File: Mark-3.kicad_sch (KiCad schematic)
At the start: 11 parts

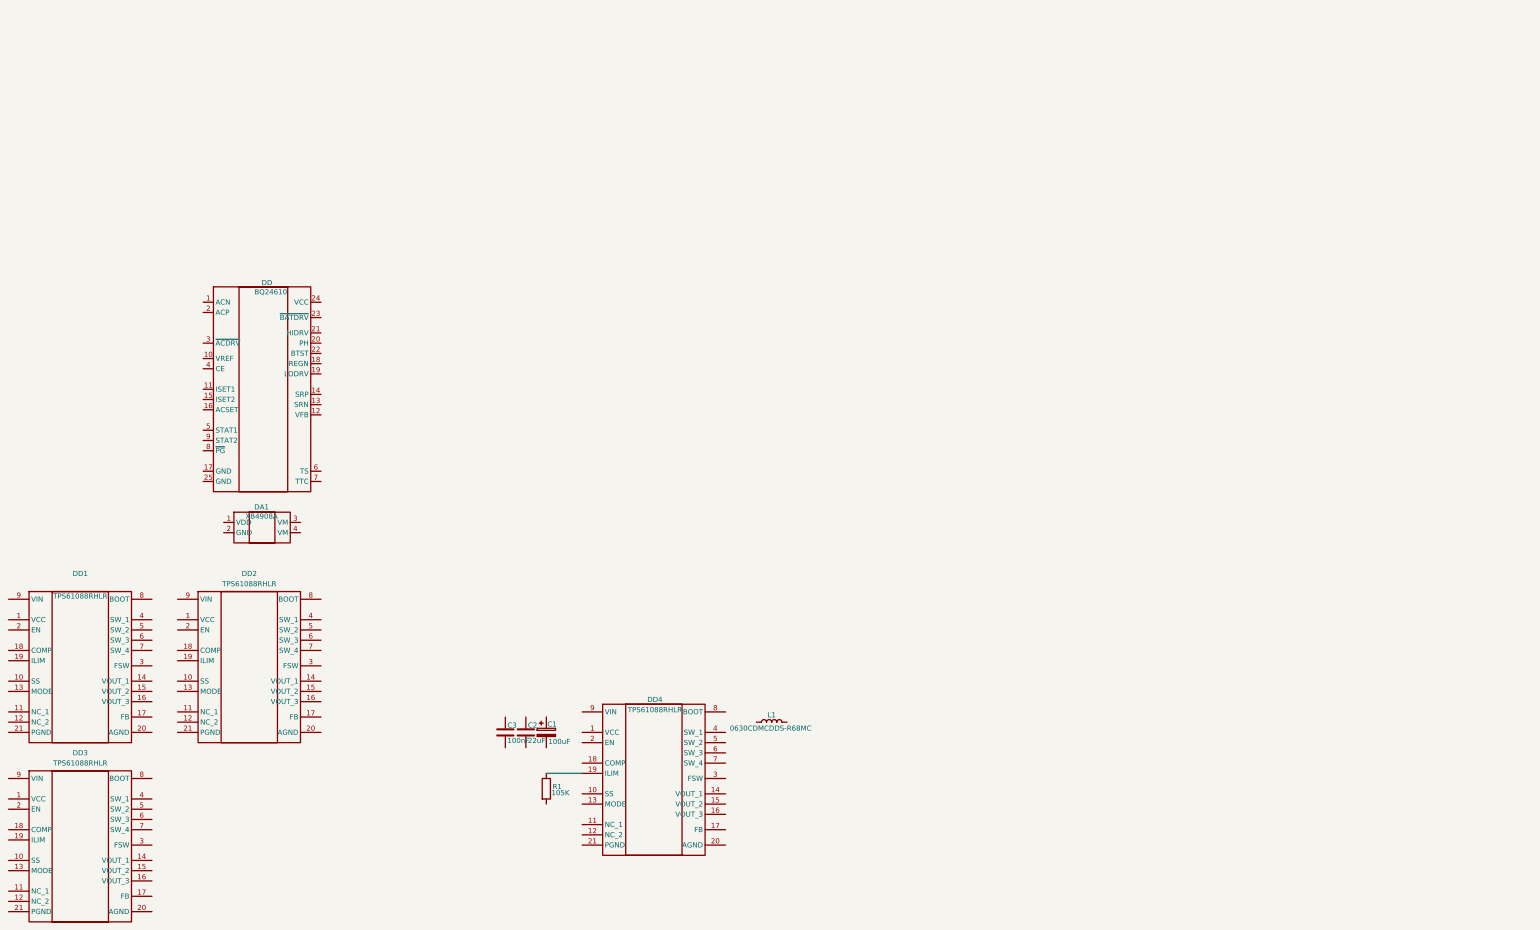
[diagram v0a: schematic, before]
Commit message: DC-DC and battery protection circuit done, partly done charger module
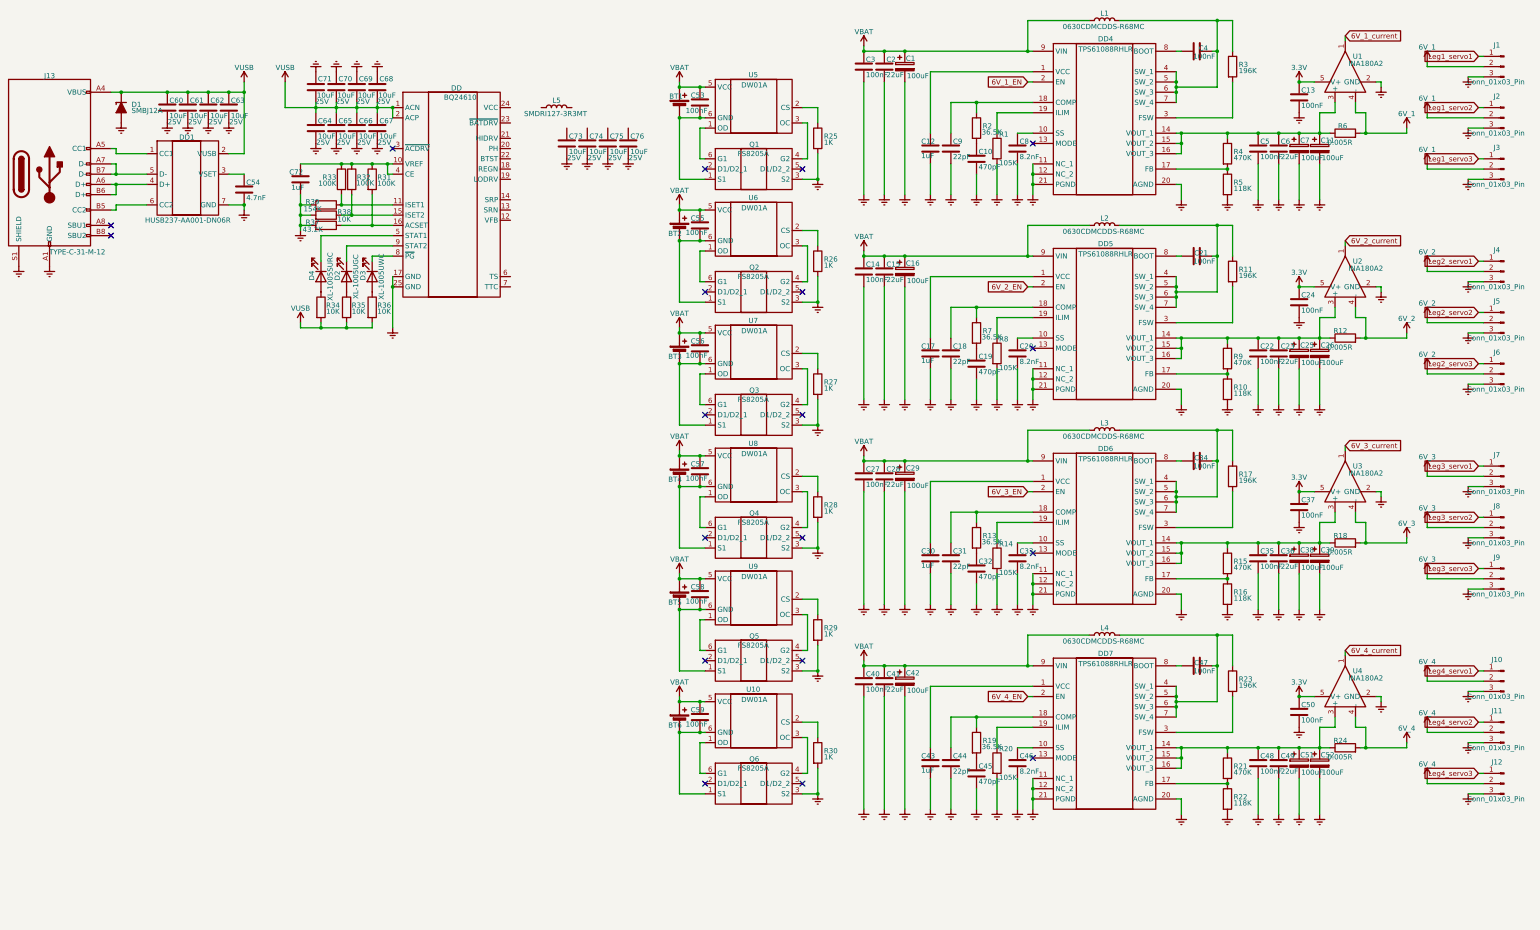
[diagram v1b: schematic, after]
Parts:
- removed DA1: XB4908A, XB4908A:XB4908A, symbol XB4908A:XB4908A
- removed DD1, DD2, DD3: TPS61088RHLR, TPS61088RHLR:TPS61088RHLR, symbol TPS61088RHLR:TPS61088RHLR
- added BT1, BT2, BT3, BT4, BT5, BT6: Battery_Cell, Battery:BatteryHolder_Keystone_1042_1x18650, symbol Device:Battery_Cell
- added C10, C19, C32, C45: 470pF, Capacitor_SMD:C_0402_1005Metric, symbol Device:C
- added C11, C16, C25, C26, C29, C38, C39, C42, C51, C52, C7: 100uF, Capacitor_Tantalum_SMD:CP_EIA-3528-21_Kemet-B, symbol Device:C_Polarized
- added C12, C17, C30, C43, C72: 1uF, Capacitor_SMD:C_0402_1005Metric, symbol Device:C
- added C13, C14, C21, C22, C24, C27, C34, C35, C37, C4, C40, C47, C48, C5, C50, C53, C55, C56, C57, C58, C59: 100nF, Capacitor_SMD:C_0402_1005Metric, symbol Device:C
- added C15, C23, C28, C36, C41, C49, C6: 22uF, Capacitor_SMD:C_0805_2012Metric, symbol Device:C
- added C18, C31, C44, C9: 22pF, Capacitor_SMD:C_0402_1005Metric, symbol Device:C
- added C20, C33, C46, C8: 8.2nF, Capacitor_SMD:C_0402_1005Metric, symbol Device:C
- added C54: 4.7nF, Capacitor_SMD:C_0402_1005Metric, symbol Device:C
- added C60, C61, C62, C63, C64, C65, C66, C67, C68, C69, C70, C71, C73, C74, C75, C76: 10uF, Capacitor_SMD:C_0805_2012Metric, symbol Device:C
- added D1: SMBJ12A, PCM_Diode_SMD_AKL:D_SMB, symbol PCM_Diode_TVS_AKL:SMBJ12A
- added D2: XL-1005UGC, LED_SMD:LED_0402_1005Metric, symbol Device:LED
- added D3: XL-1005UWC, LED_SMD:LED_0402_1005Metric, symbol Device:LED
- added D4: XL-1005SURC, LED_SMD:LED_0402_1005Metric, symbol Device:LED
- added DD1: HUSB237-AA001-DN06R, HUSB237-AA001-DN06R:HUSB237-AA001-DN06R, symbol HUSB237-AA001-DN06R:HUSB237-AA001-DN06R
- added DD5, DD6, DD7: TPS61088RHLR, TPS61088RHLR:TPS61088RHLR, symbol TPS61088RHLR:TPS61088RHLR
- added J1, J10, J11, J12, J2, J3, J4, J5, J6, J7, J8, J9: Conn_01x03_Pin, Connector_PinHeader_2.54mm:PinHeader_1x03_P2.54mm_Vertical, symbol Connector:Conn_01x03_Pin
- added J13: TYPE-C-31-M-12, Connector_USB:USB_C_Receptacle_G-Switch_GT-USB-7010ASV, symbol Connector:USB_C_Receptacle_USB2.0_16P
- added L2, L3, L4: 0630CDMCDDS-R68MC, Inductor_SMD:L_Sunlord_MWSA0603S, symbol Device:L
- added L5: SMDRI127-3R3MT, Inductor_SMD:L_SXN_SMDRI127, symbol Device:L
- added Q1, Q2, Q3, Q4, Q5, Q6: FS8205A, FS8205A:FS8205A, symbol FS8205A:FS8205A
- added R10, R16, R22, R5: 118K, PCM_Resistor_SMD_AKL:R_0402_1005Metric, symbol Device:R
- added R11, R17, R23, R3: 196K, PCM_Resistor_SMD_AKL:R_0402_1005Metric, symbol Device:R
- added R12, R18, R24, R6: 0.005R, PCM_Resistor_SMD_AKL:R_1206_3216Metric, symbol Device:R
- added R13, R19, R2, R7: 36.5K, PCM_Resistor_SMD_AKL:R_0402_1005Metric, symbol Device:R
- added R14, R20, R8: 105K, PCM_Resistor_SMD_AKL:R_0402_1005Metric, symbol Device:R
- added R15, R21, R4, R9: 470K, PCM_Resistor_SMD_AKL:R_0402_1005Metric, symbol Device:R
- added R25, R26, R27, R28, R29, R30: 1K, PCM_Resistor_SMD_AKL:R_0402_1005Metric, symbol Device:R
- added R31, R32, R33: 100K, PCM_Resistor_SMD_AKL:R_0402_1005Metric, symbol Device:R
- added R34, R35, R36, R38: 10K, PCM_Resistor_SMD_AKL:R_0402_1005Metric, symbol Device:R
- added R37: 43.2K, PCM_Resistor_SMD_AKL:R_0402_1005Metric, symbol Device:R
- added R39: 154K, PCM_Resistor_SMD_AKL:R_0402_1005Metric, symbol Device:R
- added U1, U2, U3, U4: INA180A2, Package_TO_SOT_SMD:SOT-23-5, symbol Amplifier_Current:INA180A2
- added U10, U5, U6, U7, U8, U9: DW01A, Package_TO_SOT_SMD:SOT-23-6, symbol Battery_Management:DW01A
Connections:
- net VBAT: now reaches L1.1
- net VBAT: now also C1.1, C2.1, C3.1, DD4.9 (VIN), BT1.1 (+), BT2.1 (+), BT3.1 (+), BT4.1 (+), BT5.1 (+), BT6.1 (+), C14.1, C15.1, C16.1, C27.1, C28.1, C29.1, C40.1, C41.1, C42.1, C53.1, C55.1, C56.1, C57.1, C58.1, C59.1, DD5.9 (VIN), DD6.9 (VIN), DD7.9 (VIN), L2.1, L3.1, L4.1, U10.5 (VCC), U5.5 (VCC), U6.5 (VCC), U7.5 (VCC), U8.5 (VCC), U9.5 (VCC)
- net at L1.2: now also DD4.4 (SW_1), DD4.5 (SW_2), DD4.6 (SW_3), DD4.7 (SW_4), C4.2, R3.1
- net at DD4.1 (VCC): now also C12.1
- net at DD4.10 (SS): now also C8.1
- net Earth: now reaches DD4.11 (NC_1)
- net Earth: now also C1.2, C2.2, C3.2, DD.17 (GND), DD.25 (GND), DD4.12 (NC_2), DD4.20 (AGND), DD4.21 (PGND), R1.2, C10.2, C11.2, C12.2, C13.2, C14.2, C15.2, C16.2, C17.2, C18.2, C19.2, C20.2, C22.2, C23.2, C24.2, C25.2, C26.2, C27.2, C28.2, C29.2, C30.2, C31.2, C32.2, C33.2, C35.2, C36.2, C37.2, C38.2, C39.2, C40.2, C41.2, C42.2, C43.2, C44.2, C45.2, C46.2, C48.2, C49.2, C5.2, C50.2, C51.2, C52.2, C54.2, C6.2, C60.2, C61.2, C62.2, C63.2, C64.2, C65.2, C66.2, C67.2, C68.2, C69.2, C7.2, C70.2, C71.2, C72.2, C73.2, C74.2, C75.2, C76.2, C8.2, C9.2, D1.2 (A), DD1.7 (GND), DD5.11 (NC_1), DD5.12 (NC_2), DD5.20 (AGND), DD5.21 (PGND), DD6.11 (NC_1), DD6.12 (NC_2), DD6.20 (AGND), DD6.21 (PGND), DD7.11 (NC_1), DD7.12 (NC_2), DD7.20 (AGND), DD7.21 (PGND), J1.3 (Pin_3), J10.3 (Pin_3), J11.3 (Pin_3), J12.3 (Pin_3), J13.A1 (GND), J13.A12 (GND), J13.B1 (GND), J13.B12 (GND), J13.S1 (SHIELD), J2.3 (Pin_3), J3.3 (Pin_3), J4.3 (Pin_3), J5.3 (Pin_3), J6.3 (Pin_3), J7.3 (Pin_3), J8.3 (Pin_3), J9.3 (Pin_3), Q1.3 (S2), Q2.3 (S2), Q3.3 (S2), Q4.3 (S2), Q5.3 (S2), Q6.3 (S2), R10.2, R14.2, R16.2, R20.2, R22.2, R25.2, R26.2, R27.2, R28.2, R29.2, R30.2, R37.2, R38.2, R39.2, R5.2, R8.2, U1.2 (GND), U2.2 (GND), U3.2 (GND), U4.2 (GND)
- net at DD4.14 (VOUT_1): now also DD4.15 (VOUT_2), DD4.16 (VOUT_3), C11.1, C5.1, C6.1, C7.1, R4.1, R6.1, U1.3 (+)
- net at DD4.17 (FB): now also R4.2, R5.1
- net at DD4.18 (COMP): now also C9.1, R2.1
- net 6V_1_EN: now reaches DD4.2 (EN)
- net at DD4.3 (FSW): now also R3.2
- net at DD4.8 (BOOT): now also C4.1
- net VUSB: now reaches DD.1 (ACN)
- net VUSB: now also DD.2 (ACP), C60.1, C61.1, C62.1, C63.1, C64.1, C65.1, C66.1, C67.1, C68.1, C69.1, C70.1, C71.1, D1.1 (K), DD1.2 (VUSB), J13.A4 (VBUS), J13.A9 (VBUS), J13.B4 (VBUS), J13.B9 (VBUS), R34.2, R35.2, R36.2
- net at DD.10 (VREF): now also DD.4 (CE), C72.1, R31.1, R32.1, R33.1
- net at DD.11 (ISET1): now also R33.2, R39.1
- net at DD.15 (ISET2): now also R32.2, R38.1
- net at DD.16 (ACSET): now also R31.2, R37.1
- net at DD.5 (STAT1): now also D4.1 (K)
- net at DD.8 (~{PG}): now also D3.1 (K)
- net at DD.9 (STAT2): now also D2.1 (K)
- new net: BT2.2 (-), C55.2, Q2.1 (S1), U6.6 (GND)
- new net: Q2.4 (G2), U6.3 (OC)
- new net: Q2.6 (G1), U6.1 (OD)
- new net: BT5.2 (-), C58.2, Q5.1 (S1), U9.6 (GND)
- new net: Q5.4 (G2), U9.3 (OC)
- new net: Q5.6 (G1), U9.1 (OD)
- new net: D3.2 (A), R36.1
- new net: C22.1, C23.1, C25.1, C26.1, DD5.14 (VOUT_1), DD5.15 (VOUT_2), DD5.16 (VOUT_3), R12.1, R9.1, U2.3 (+)
- new net: DD5.17 (FB), R10.1, R9.2
- new net: BT4.2 (-), C57.2, Q4.1 (S1), U8.6 (GND)
- new net: C48.1, C49.1, C51.1, C52.1, DD7.14 (VOUT_1), DD7.15 (VOUT_2), DD7.16 (VOUT_3), R21.1, R24.1, U4.3 (+)
- new net: Q3.6 (G1), U7.1 (OD)
- new net: R27.1, U7.2 (CS)
- new net: Q3.4 (G2), U7.3 (OC)
- new net: BT3.2 (-), C56.2, Q3.1 (S1), U7.6 (GND)
- new net: C45.1, R19.2
- new net: BT6.2 (-), C59.2, Q6.1 (S1), U10.6 (GND)
- new net: Q6.4 (G2), U10.3 (OC)
- new net: Q6.6 (G1), U10.1 (OD)
- new net: R30.1, U10.2 (CS)
- new net: Q4.6 (G1), U8.1 (OD)
- new net: R28.1, U8.2 (CS)
- new net: Q4.4 (G2), U8.3 (OC)
- new net: C30.1, DD6.1 (VCC)
- new net: C33.1, DD6.10 (SS)
- new net: C35.1, C36.1, C38.1, C39.1, DD6.14 (VOUT_1), DD6.15 (VOUT_2), DD6.16 (VOUT_3), R15.1, R18.1, U3.3 (+)
- new net: DD6.17 (FB), R15.2, R16.1
- new net: C31.1, DD6.18 (COMP), R13.1
- new net: DD6.19 (ILIM), R14.1
- new net: DD6.3 (FSW), R17.2
- new net: C34.2, DD6.4 (SW_1), DD6.5 (SW_2), DD6.6 (SW_3), DD6.7 (SW_4), L3.2, R17.1
- new net: C34.1, DD6.8 (BOOT)
- new net: BT1.2 (-), C53.2, Q1.1 (S1), U5.6 (GND)
- new net: C21.2, DD5.4 (SW_1), DD5.5 (SW_2), DD5.6 (SW_3), DD5.7 (SW_4), L2.2, R11.1
- new net: R29.1, U9.2 (CS)
- new net: C32.1, R13.2
- new net: DD5.19 (ILIM), R8.1
- new net: D4.2 (A), R34.1
- new net: C44.1, DD7.18 (COMP), R19.1
- new net: R25.1, U5.2 (CS)
- new net: C43.1, DD7.1 (VCC)
- new net: C10.1, R2.2
- new net: C21.1, DD5.8 (BOOT)
- new net: DD5.3 (FSW), R11.2
- new net: DD7.19 (ILIM), R20.1
- new net: C47.2, DD7.4 (SW_1), DD7.5 (SW_2), DD7.6 (SW_3), DD7.7 (SW_4), L4.2, R23.1
- new net: DD7.3 (FSW), R23.2
- new net: Q1.4 (G2), U5.3 (OC)
- new net: Q1.6 (G1), U5.1 (OD)
- new net: DD7.17 (FB), R21.2, R22.1
- new net: C46.1, DD7.10 (SS)
- new net: C47.1, DD7.8 (BOOT)
- new net: D2.2 (A), R35.1
- new net: C17.1, DD5.1 (VCC)
- new net: C20.1, DD5.10 (SS)
- new net: C18.1, DD5.18 (COMP), R7.1
- new net: R26.1, U6.2 (CS)
- new net: C54.1, DD1.3 (VSET)
- new net: DD1.1 (CC1), J13.A5 (CC1)
- new net: DD1.4 (D+), J13.A6 (D+), J13.B6 (D+)
- new net: DD1.5 (D-), J13.A7 (D-), J13.B7 (D-)
- new net: DD1.6 (CC2), J13.B5 (CC2)
- new net: C19.1, R7.2
- new net 3.3V: C13.1, C24.1, C37.1, C50.1, U1.5 (V+), U2.5 (V+), U3.5 (V+), U4.5 (V+)
- new net 6V_1: J1.2 (Pin_2), J2.2 (Pin_2), J3.2 (Pin_2), R6.2, U1.4 (-)
- new net 6V_1_current: U1.1
- new net 6V_2: J4.2 (Pin_2), J5.2 (Pin_2), J6.2 (Pin_2), R12.2, U2.4 (-)
- new net 6V_2_EN: DD5.2 (EN)
- new net 6V_2_current: U2.1
- new net 6V_3: J7.2 (Pin_2), J8.2 (Pin_2), J9.2 (Pin_2), R18.2, U3.4 (-)
- new net 6V_3_EN: DD6.2 (EN)
- new net 6V_3_current: U3.1
- new net 6V_4: J10.2 (Pin_2), J11.2 (Pin_2), J12.2 (Pin_2), R24.2, U4.4 (-)
- new net 6V_4_EN: DD7.2 (EN)
- new net 6V_4_current: U4.1
- new net Leg1_servo1: J1.1 (Pin_1)
- new net Leg1_servo2: J2.1 (Pin_1)
- new net Leg1_servo3: J3.1 (Pin_1)
- new net Leg2_servo1: J4.1 (Pin_1)
- new net Leg2_servo2: J5.1 (Pin_1)
- new net Leg2_servo3: J6.1 (Pin_1)
- new net Leg3_servo1: J7.1 (Pin_1)
- new net Leg3_servo2: J8.1 (Pin_1)
- new net Leg3_servo3: J9.1 (Pin_1)
- new net Leg4_servo1: J10.1 (Pin_1)
- new net Leg4_servo2: J11.1 (Pin_1)
- new net Leg4_servo3: J12.1 (Pin_1)
- no-connect marks 0 -> 19
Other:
- moved on the sheet: C1, C2, C3, DD, DD4, L1, R1

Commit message: Partly done placement, moving forward to GPIO assigment with placement spec
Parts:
- removed C74, C75, C76: 10uF, Capacitor_SMD:C_0805_2012Metric, symbol Device:C
- added AE1: Antenna_Shield, RF_Antenna:Texas_SWRA117D_2.4GHz_Right, symbol Device:Antenna_Shield
- added C1, C39, C40, C42, C43, C68: 100nF, Capacitor_SMD:C_0201_0603Metric, symbol Device:C
- added C10, C41, C5, C52: 22pF, Capacitor_SMD:C_0201_0603Metric, symbol Device:C
- added C11, C13, C14, C16, C18, C19, C2, C21, C3, C32, C4, C45, C46, C50, C51, C53, C55, C59, C67, C69, C71: 4.7uF, Capacitor_SMD:C_0201_0603Metric, symbol Device:C
- added C20, C34: 10nF, Capacitor_SMD:C_0201_0603Metric, symbol Device:C
- added C29: 33nF, Capacitor_SMD:C_0201_0603Metric, symbol Device:C
- added C33: 2.2nF, Capacitor_SMD:C_0201_0603Metric, symbol Device:C
- added C35, C62, C70, C72: 1.5pF, Capacitor_SMD:C_0201_0603Metric, symbol Device:C
- added C36: 4.7pF, Capacitor_SMD:C_0201_0603Metric, symbol Device:C
- added C37: 1nF, Capacitor_SMD:C_0201_0603Metric, symbol Device:C
- added C38: 1pF, Capacitor_SMD:C_0201_0603Metric, symbol Device:C
- added C44: 56nF, Capacitor_SMD:C_0402_1005Metric, symbol Device:C
- added C47, C54: 1uF, Capacitor_SMD:C_0402_1005Metric, symbol Device:C
- added C48, C49, C56, C57: 100nF, Capacitor_SMD:C_0402_1005Metric, symbol Device:C
- added C58: 0.3pF, Capacitor_SMD:C_0201_0603Metric, symbol Device:C
- added C6, C8: 22uF, Capacitor_SMD:C_0402_1005Metric, symbol Device:C
- added C60, C61, C65, C66: 10uF, Capacitor_SMD:C_0805_2012Metric, symbol Device:C
- added C63: 220pF, Capacitor_SMD:C_0201_0603Metric, symbol Device:C
- added C64: 22pF, Capacitor_SMD:C_0402_1005Metric, symbol Device:C
- added D1, D10, D11, D12, D14, D15, D16, D2, D3, D4, D5, D6, D7, D8, D9: XL-1005UWC, LED_SMD:LED_0402_1005Metric, symbol Device:LED
- added D20: BAT54, PCM_Package_TO_SOT_SMD_AKL:SOT-23, symbol PCM_Diode_Schottky_AKL:BAT54
- added DA1: RFX2401C, RFX2401C:RFX2401C, symbol RFX2401C:RFX2401C
- added DD1: W25Q16JVUXIQ_TR, W25Q16JVUXIQ:W25Q16JVUXIQ, symbol W25Q16JVUXIQ_TR:W25Q16JVUXIQ_TR
- added DD2: BCT2057ELT33, BCT2057ELTAJ:BCT2057ELTAJ, symbol BCT2057ELTAJ:BCT2057ELTAJ-TR
- added DD4: nRF24L01P, Package_DFN_QFN:QFN-20-1EP_4x4mm_P0.5mm_EP2.5x2.5mm, symbol RF:nRF24L01P
- added DD5: RP2350B, RP2350B:QFN40P1000X1000X90-81N-D, symbol RP2350B:RP2350B
- added DD7: LSM6DS3, Package_LGA:LGA-14_3x2.5mm_P0.5mm_LayoutBorder3x4y, symbol Sensor_Motion:LSM6DS3
- added J1: Conn_01x02_Pin, Connector_PinHeader_2.54mm:PinHeader_1x02_P2.54mm_Vertical, symbol Connector:Conn_01x02_Pin
- added J3: TYPE-C-31-M-12, Connector_USB:USB_C_Receptacle_GCT_USB4105-xx-A_16P_TopMnt_Horizontal, symbol Connector:USB_C_Receptacle_USB2.0_16P
- added L1: VHF160808H33NJT, Inductor_SMD:L_0603_1608Metric, symbol Device:L
- added L2: FHW0603UF3R3JST, Inductor_SMD:L_0603_1608Metric, symbol Device:L
- added L3: 8.2nH, Inductor_SMD:L_0201_0603Metric, symbol Device:L
- added L4: 3.9nH, Inductor_SMD:L_0201_0603Metric, symbol Device:L
- added L5: 2.7nH, Inductor_SMD:L_0201_0603Metric, symbol Device:L
- added L7, L8: 2.4nH, Inductor_SMD:L_0201_0603Metric, symbol Device:L
- added Q1, Q2: HSBA4052, Package_DFN_QFN:PQFN-8-EP_6x5mm_P1.27mm_Generic, symbol Device:Q_NMOS
- added R1, R10, R11, R12, R13, R16, R18, R2, R21, R3, R4, R5, R6, R7, R8: 1K, PCM_Resistor_SMD_AKL:R_0402_1005Metric, symbol Device:R
- added R14, R15: 5.1K, PCM_Resistor_SMD_AKL:R_0402_1005Metric, symbol Device:R
- added R17, R37: 1M, PCM_Resistor_SMD_AKL:R_0201_0603Metric, symbol Device:R
- added R19, R20: 27R, PCM_Resistor_SMD_AKL:R_0201_0603Metric, symbol Device:R
- added R22: 22K, PCM_Resistor_SMD_AKL:R_0201_0603Metric, symbol Device:R
- added R32, R33, R38, R39, R40, R9: 1K, PCM_Resistor_SMD_AKL:R_0201_0603Metric, symbol Device:R
- added R34: 20K, PCM_Resistor_SMD_AKL:R_0201_0603Metric, symbol Device:R
- added R35: 10R, PCM_Resistor_SMD_AKL:R_0402_1005Metric, symbol Device:R
- added R36, R45, R46: 10K, PCM_Resistor_SMD_AKL:R_0201_0603Metric, symbol Device:R
- added R41: 100R, PCM_Resistor_SMD_AKL:R_0402_1005Metric, symbol Device:R
- added R42: 9.31K, PCM_Resistor_SMD_AKL:R_0402_1005Metric, symbol Device:R
- added R43: 430K, PCM_Resistor_SMD_AKL:R_0402_1005Metric, symbol Device:R
- added R44: 0.010R, PCM_Resistor_SMD_AKL:R_2512_6332Metric_Pad1.40x3.35mm, symbol Device:R
- added R47, R48: 200K, PCM_Resistor_SMD_AKL:R_0402_1005Metric, symbol Device:R
- added SW1, SW2: KMR221GLFS, Button_Switch_SMD:SW_SPST_PTS810, symbol Switch:SW_Push
- added TP1, TP10, TP11, TP12, TP2, TP3, TP4, TP5, TP6, TP7, TP8, TP9: TestPoint, TestPoint:TestPoint_Pad_D1.0mm, symbol Connector:TestPoint
- added U1: USBLC6-2SC6, Package_TO_SOT_SMD:SOT-23-6, symbol Power_Protection:USBLC6-2SC6
- added Y1, Y2: 16MHz, Crystal:Crystal_SMD_3225-4Pin_3.2x2.5mm, symbol Device:Crystal_GND24
- C73: value 10uF -> 1.5pF; footprint Capacitor_SMD:C_0805_2012Metric -> Capacitor_SMD:C_0201_0603Metric; JLCPCB part C5674 -> (none); Voltage 25V -> (none)
- renumbered C10 to C100, C19 to C101, C32 to C102, C45 to C103, C8 to C104, C20 to C105, C33 to C106, C46 to C107, C4 to C108, C21 to C109, C34 to C110, C47 to C111, C5 to C112, C22 to C113, C35 to C114, C48 to C115, C6 to C116, C23 to C117, C36 to C118, C49 to C119, C62 to C12, C13 to C120, C7 to C121, C24 to C122, C25 to C123, C37 to C124, C38 to C125, C50 to C126, C51 to C127, C11 to C128, C26 to C129, C39 to C130, C52 to C131, C63 to C15, C54 to C17, C72 to C22, C71 to C23, C64 to C24, C70 to C25, C65 to C26, C69 to C27, C66 to C28, C68 to C30, C67 to C31, C60 to C7, C53 to C74, C55 to C75, C56 to C76, C57 to C77, C58 to C78, C59 to C79, C3 to C80, C14 to C81, C27 to C82, C40 to C83, C2 to C84, C15 to C85, C28 to C86, C41 to C87, C1 to C88, C16 to C89, C61 to C9, C29 to C90, C42 to C91, C12 to C92, C17 to C93, C30 to C94, C43 to C95, C9 to C96, C18 to C97, C31 to C98, C44 to C99, D1 to D13, D4 to D17, D2 to D18, D3 to D19, DD6 to DD10, DD7 to DD11, DD1 to DD3, DD to DD6, DD4 to DD8, DD5 to DD9, J7 to J10, J8 to J11, J9 to J12, J10 to J13, J11 to J14, J12 to J15, J13 to J2, J1 to J4, J2 to J5, J3 to J6, J4 to J7, J5 to J8, J6 to J9, L2 to L10, L3 to L11, L4 to L12, L5 to L6, L1 to L9, Q1 to Q3, Q2 to Q4, Q3 to Q5, Q4 to Q6, Q5 to Q7, Q6 to Q8, R34 to R23, R39 to R24, R38 to R25, R37 to R26, R33 to R27, R35 to R28, R32 to R29, R31 to R30, R36 to R31, R25 to R49, R26 to R50, R27 to R51, R28 to R52, R29 to R53, R30 to R54, R2 to R55, R7 to R56, R13 to R57, R19 to R58, R1 to R59, R8 to R60, R14 to R61, R20 to R62, R4 to R63, R5 to R64, R9 to R65, R10 to R66, R15 to R67, R16 to R68, R21 to R69, R22 to R70, R3 to R71, R11 to R72, R17 to R73, R23 to R74, R6 to R75, R12 to R76, R18 to R77, R24 to R78, U3 to U10, U4 to U11, U5 to U2, U6 to U3, U7 to U4, U8 to U5, U9 to U6, U10 to U7, U1 to U8, U2 to U9
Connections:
- net 3.3V: now also C1.1, C11.1, C14.1, C3.1, C32.1, C34.1, C37.1, C39.1, C40.1, C42.1, C43.1, C45.1, C46.1, C50.1, C51.1, C53.1, C55.1, C59.1, C63.1, C67.1, C68.1, C69.1, C71.1, C8.1, DA1.16 (VDD_2), DD1.8 (VCC), DD2.1 (OUT), DD4.15 (VDD), DD4.18 (VDD), DD4.7 (VDD), DD5.15 (IOVDD_2), DD5.24 (IOVDD_3), DD5.29 (IOVDD_4), DD5.41 (IOVDD_5), DD5.5 (IOVDD_1), DD5.50 (IOVDD_6), DD5.60 (IOVDD_7), DD5.64 (VREG_VIN), DD5.68 (USB_OTP_VDD), DD5.69 (QSPI_IOVDD), DD5.76 (IOVDD_8), DD7.5 (VDDIO), DD7.8 (VDD), L1.1, R12.2, R36.2, TP1.1
- net 6V_1: now also R2.2
- net 6V_1_EN: now also DD5.45 (GPIO36)
- net 6V_1_current: now also DD5.52 (GPIO41_ADC1)
- net 6V_2: now also R4.2
- net 6V_2_EN: now also DD5.46 (GPIO37)
- net 6V_2_current: now also DD5.53 (GPIO42_ADC2)
- net 6V_3: now also R7.2
- net 6V_3_EN: now also DD5.47 (GPIO38)
- net 6V_3_current: now also DD5.54 (GPIO43_ADC3)
- net 6V_4: now also R10.2
- net 6V_4_EN: now also DD5.48 (GPIO39)
- net 6V_4_current: now also DD5.55 (GPIO44_ADC4)
- net Earth: now also AE1.2 (Shield), C1.2, C10.2, C11.2, C13.2, C14.2, C16.2, C18.2, C19.1, C2.2, C20.2, C21.1, C29.2, C3.2, C32.2, C33.2, C34.2, C36.2, C37.2, C38.2, C39.2, C4.2, C40.2, C41.2, C42.2, C43.2, C44.2, C45.2, C46.2, C47.1, C49.1, C5.2, C50.2, C51.2, C52.2, C53.2, C54.1, C55.2, C56.2, C58.2, C59.2, C6.2, C60.2, C61.2, C62.2, C63.2, C65.2, C66.2, C67.2, C68.2, C69.2, C70.2, C71.2, C72.2, C8.2, D1.1 (K), D10.1 (K), D11.1 (K), D12.1 (K), D14.1 (K), D15.1 (K), D16.1 (K), D2.1 (K), D3.1 (K), D4.1 (K), D5.1 (K), D6.1 (K), D7.1 (K), D8.1 (K), D9.1 (K), DA1.11 (GND_5), DA1.17 (GND_6), DA1.2 (GND_1), DA1.3 (GND_2), DA1.8 (GND_3), DA1.9 (GND_4), DD1.4 (GND), DD2.0 (EP), DD2.3 (GND), DD4.14 (VSS), DD4.17 (VSS), DD4.20 (VSS), DD4.21 (PAD), DD4.8 (VSS), DD5.62 (VREG_PGND), DD5.81 (GND), DD7.6 (GND), DD7.7 (GND), J3.A1 (GND), J3.A12 (GND), J3.B1 (GND), J3.B12 (GND), J3.S1 (SHIELD), Q2.1 (S), Q2.2 (S), Q2.3 (S), R14.2, R15.2, R22.1, R34.2, R38.1, R39.1, R43.2, R46.1, R48.2, SW1.1, SW2.1, TP2.1, U1.2 (GND), Y1.2, Y1.4, Y2.2, Y2.4
- net Leg1_servo1: now also DD5.79 (GPIO2)
- net Leg1_servo2: now also DD5.80 (GPIO3)
- net Leg1_servo3: now also DD5.1 (GPIO4)
- net Leg2_servo1: now also DD5.2 (GPIO5)
- net Leg2_servo2: now also DD5.3 (GPIO6)
- net Leg2_servo3: now also DD5.4 (GPIO7)
- net Leg3_servo1: now also DD5.6 (GPIO8)
- net Leg3_servo2: now also DD5.7 (GPIO9)
- net Leg3_servo3: now also DD5.8 (GPIO10)
- net Leg4_servo1: now also DD5.9 (GPIO11)
- net Leg4_servo2: now also DD5.11 (GPIO12)
- net Leg4_servo3: now also DD5.12 (GPIO13)
- net VBAT: now also DD6.13 (SRN), C2.1, C4.1, C57.2, C60.1, C61.1, C64.1, C65.1, C66.1, DD2.6 (IN), J1.1 (Pin_1), R44.2, R45.2, R47.1
- net VUSB: now also C47.2, Q1.5 (D), R35.1
- net at L6.1: now also C48.2, Q1.1 (S), Q1.2 (S), Q1.3 (S), Q2.5 (D)
- net at L6.2: now also DD6.14 (SRP), C56.1, C57.1, R44.1
- net VREF: now reaches C22.1, DD6.10 (VREF), DD6.4 (CE), R27.1, R29.1, R30.1
- net VREF: now also R42.2
- net at DD6.12 (VFB): now also C64.2, R47.2, R48.1
- net at DD6.18 (REGN): now also C54.2, D20.1 (A)
- net at DD6.19 (LODRV): now also Q2.4 (G)
- net at DD6.21 (HIDRV): now also Q1.4 (G)
- net at DD6.22 (BTST): now also C48.1, D20.3 (K)
- net at DD6.24 (VCC): now also R35.2
- net at DD6.6 (TS): now also R41.1
- net at DD6.7 (TTC): now also C44.1
- net at C73.1: now also AE1.1 (A), L8.2
- new net: C19.2, C21.2, DD5.59 (ADC_AVDD), DD5.61 (VREG_AVDD), L1.2
- new net: D6.2 (A), R6.1
- new net: R40.2, SW2.2
- new net: C13.1, C16.1, C18.1, C20.1, DD5.10 (DVDD_1), DD5.32 (DVDD_2), DD5.51 (DVDD_3), DD5.65 (VREG_FB), L2.2
- new net: D15.2 (A), R18.1
- new net: D12.2 (A), R13.1
- new net: D16.2 (A), R21.1
- new net: DD5.25 (GPIO24), TP5.1
- new net: DD5.26 (GPIO25), TP6.1
- new net: DD5.27 (GPIO26), TP7.1
- new net: C52.1, DD5.30 (XIN), R37.1, Y2.1
- new net: C41.1, DD5.31 (XOUT), R37.2, Y2.3
- new net: DD5.33 (SWCLK), TP12.1
- new net: DD5.34 (SWDIO), TP11.1
- new net: DD5.35 (RUN), R36.1, R40.1
- new net: DD5.56 (GPIO45_ADC5), TP8.1
- new net: DD5.57 (GPIO46_ADC6), TP9.1
- new net: DD5.58 (GPIO47_ADC7), TP10.1
- new net: DD5.63 (VREG_LX), L2.1
- new net: DD5.77 (GPIO0), TP3.1
- new net: DD5.78 (GPIO1), TP4.1
- new net: D9.2 (A), R10.1
- new net: DD4.13 (ANT2), L3.1, L4.1
- new net: C35.1, L4.2
- new net: C5.1, DD4.9 (XC2), R17.1, Y1.1
- new net: C10.1, DD4.10 (XC1), R17.2, Y1.3
- new net: D11.2 (A), R12.1
- new net: DD2.4 (EN), J1.2 (Pin_2)
- new net: C35.2, C38.1, DA1.4 (TXRX)
- new net: C58.1, C62.1, DA1.10 (ANT), L7.1
- new net: C70.1, C72.1, L7.2, L8.1
- new net: R9.2, SW1.2
- new net: D14.2 (A), R16.1
- new net: DA1.6 (RXEN), R33.2, R34.1
- new net: D4.2 (A), R4.1
- new net: D5.2 (A), R5.1
- new net: D2.2 (A), R2.1
- new net: C49.2, R41.2, R42.1, R43.1
- new net: DD7.2 (SDX), R38.2
- new net: DD7.3 (SCX), R39.2
- new net: J3.A5 (CC1), R14.1
- new net: DD4.12 (ANT1), L3.2, L5.1
- new net: D10.2 (A), R11.1
- new net: J3.B5 (CC2), R15.1
- new net: D8.2 (A), R8.1
- new net: DA1.5 (TXEN), R32.2
- new net: D7.2 (A), R7.1
- new net: C29.1, DD4.19 (DVDD)
- new net: D3.2 (A), R3.1
- new net: DD4.16 (IREF), R22.2
- new net: D1.2 (A), R1.1
- new net +5V: C6.1, J3.A4 (VBUS), J3.A9 (VBUS), J3.B4 (VBUS), J3.B9 (VBUS), U1.5 (VBUS)
- new net BAT_ADC: DD5.49 (GPIO40_ADC0), R45.1, R46.2
- new net IMU_CS: DD5.42 (GPIO33), DD7.12 (CS)
- new net IMU_INT1: DD5.43 (GPIO34), DD7.4 (INT1)
- new net IMU_INT2: DD5.44 (GPIO35), DD7.9 (INT2)
- new net LED1: DD5.22 (GPIO22), R6.2
- new net LED2: DD5.23 (GPIO23), R1.2
- new net LVL1: DD5.13 (GPIO14), R3.2
- new net LVL2: DD5.14 (GPIO15), R5.2
- new net LVL3: DD5.16 (GPIO16), R8.2
- new net LVL4: DD5.17 (GPIO17), R11.2
- new net LVL5: DD5.18 (GPIO18), R13.2
- new net LVL6: DD5.19 (GPIO19), R16.2
- new net LVL7: DD5.20 (GPIO20), R18.2
- new net LVL8: DD5.21 (GPIO21), R21.2
- new net NRF_CE: DD4.1 (CE), DD5.39 (GPIO31), R33.1
- new net NRF_CS: DD4.2 (CSN), DD5.38 (GPIO30)
- new net NRF_IRQ: DD4.6 (IRQ), DD5.40 (GPIO32)
- new net QSPI_SCLK: DD1.6 (CLK), DD5.71 (QSPI_SCLK)
- new net QSPI_SD0: DD1.5 (DI(IO0)), DD5.72 (QSPI_SD0)
- new net QSPI_SD1: DD1.2 (DO(IO1)), DD5.74 (QSPI_SD1)
- new net QSPI_SD2: DD1.3 (IO2), DD5.73 (QSPI_SD2)
- new net QSPI_SD3: DD1.7 (IO3), DD5.70 (QSPI_SD3)
- new net QSPI_SS: DD1.1 (~{CS}), DD5.75 (QSPI_SS), R9.1
- new net SPI_MISO: DD4.5 (MISO), DD5.36 (GPIO28), DD7.1 (SDO/SA0)
- new net SPI_MOSI: DD4.4 (MOSI), DD5.28 (GPIO27), DD7.14 (SDA)
- new net SPI_SCK: DD4.3 (SCK), DD5.37 (GPIO29), DD7.13 (SCL)
- new net USB_Conn+: J3.A6 (D+), J3.B6 (D+), U1.6 (I/O1)
- new net USB_Conn-: J3.A7 (D-), J3.B7 (D-), U1.4 (I/O2)
- new net USB_ESD+: R19.2, U1.1 (I/O1)
- new net USB_ESD-: R20.2, U1.3 (I/O2)
- new net USB_R+: DD5.67 (USB_DP), R19.1
- new net USB_R-: DD5.66 (USB_DM), R20.1
- new net VDD_PA: C33.1, C36.1, DD4.11 (VDD_PA), L5.2, R32.1
- no-connect marks 19 -> 24
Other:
- company: (none) -> MADJOGGER
- title: (none) -> Mark 3
- moved on the sheet: BT1, BT2, BT3, BT4, BT5, BT6, C100, C101, C102, C103, C104, C105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

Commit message: rev0 ready
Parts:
- removed TP10, TP11, TP12: TestPoint, TestPoint:TestPoint_Pad_D1.0mm, symbol Connector:TestPoint
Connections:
- net 6V_1_EN: now also DD5.11 (GPIO12); no longer DD5.45 (GPIO36)
- net 6V_1_current: now also DD5.53 (GPIO42_ADC2); no longer DD5.52 (GPIO41_ADC1)
- net 6V_2_EN: now also DD5.9 (GPIO11); no longer DD5.46 (GPIO37)
- net 6V_2_current: now also DD5.54 (GPIO43_ADC3); no longer DD5.53 (GPIO42_ADC2)
- net 6V_3_EN: now also DD5.8 (GPIO10); no longer DD5.47 (GPIO38)
- net 6V_3_current: now also DD5.55 (GPIO44_ADC4); no longer DD5.54 (GPIO43_ADC3)
- net 6V_4_EN: now also DD5.7 (GPIO9); no longer DD5.48 (GPIO39)
- net 6V_4_current: now also DD5.56 (GPIO45_ADC5); no longer DD5.55 (GPIO44_ADC4)
- net BAT_ADC: now also DD5.57 (GPIO46_ADC6); no longer DD5.49 (GPIO40_ADC0)
- net LED1: now also DD5.77 (GPIO0); no longer DD5.22 (GPIO22)
- net LED2: now also DD5.78 (GPIO1); no longer DD5.23 (GPIO23)
- net LVL1: now also DD5.12 (GPIO13); no longer DD5.13 (GPIO14)
- net LVL2: now also DD5.13 (GPIO14); no longer DD5.14 (GPIO15)
- net LVL3: now also DD5.14 (GPIO15); no longer DD5.16 (GPIO16)
- net LVL4: now also DD5.16 (GPIO16); no longer DD5.17 (GPIO17)
- net LVL5: now also DD5.17 (GPIO17); no longer DD5.18 (GPIO18)
- net LVL6: now also DD5.18 (GPIO18); no longer DD5.19 (GPIO19)
- net LVL7: now also DD5.19 (GPIO19); no longer DD5.20 (GPIO20)
- net LVL8: now also DD5.20 (GPIO20); no longer DD5.21 (GPIO21)
- net Leg1_servo1: now also DD5.40 (GPIO32); no longer DD5.79 (GPIO2)
- net Leg1_servo2: now also DD5.39 (GPIO31); no longer DD5.80 (GPIO3)
- net Leg1_servo3: now also DD5.38 (GPIO30); no longer DD5.1 (GPIO4)
- net Leg2_servo1: now also DD5.37 (GPIO29); no longer DD5.2 (GPIO5)
- net Leg2_servo2: now also DD5.36 (GPIO28); no longer DD5.3 (GPIO6)
- net Leg2_servo3: now also DD5.28 (GPIO27); no longer DD5.4 (GPIO7)
- net Leg3_servo1: now also DD5.27 (GPIO26); no longer DD5.6 (GPIO8)
- net Leg3_servo2: now also DD5.26 (GPIO25); no longer DD5.7 (GPIO9)
- net Leg3_servo3: now also DD5.25 (GPIO24); no longer DD5.8 (GPIO10)
- net Leg4_servo1: now also DD5.23 (GPIO23); no longer DD5.9 (GPIO11)
- net Leg4_servo2: now also DD5.22 (GPIO22); no longer DD5.11 (GPIO12)
- net Leg4_servo3: now also DD5.21 (GPIO21); no longer DD5.12 (GPIO13)
- net NRF_CE: now also DD5.49 (GPIO40_ADC0); no longer DD5.39 (GPIO31)
- net NRF_CS: now also DD5.46 (GPIO37); no longer DD5.38 (GPIO30)
- net NRF_IRQ: now also DD5.52 (GPIO41_ADC1); no longer DD5.40 (GPIO32)
- net SPI_MISO: now also DD5.45 (GPIO36); no longer DD5.36 (GPIO28)
- net SPI_MOSI: now also DD5.48 (GPIO39); no longer DD5.28 (GPIO27)
- net SPI_SCK: now also DD5.47 (GPIO38); no longer DD5.37 (GPIO29)
- net at TP5.1: now also DD5.1 (GPIO4); no longer DD5.25 (GPIO24)
- net at TP6.1: now also DD5.2 (GPIO5); no longer DD5.26 (GPIO25)
- net at TP7.1: now also DD5.3 (GPIO6); no longer DD5.27 (GPIO26)
- net at TP8.1: now also DD5.4 (GPIO7); no longer DD5.56 (GPIO45_ADC5)
- net at TP9.1: now also DD5.6 (GPIO8); no longer DD5.57 (GPIO46_ADC6)
- net at TP3.1: now also DD5.79 (GPIO2); no longer DD5.77 (GPIO0)
- net at TP4.1: now also DD5.80 (GPIO3); no longer DD5.78 (GPIO1)
- no-connect marks 24 -> 27
